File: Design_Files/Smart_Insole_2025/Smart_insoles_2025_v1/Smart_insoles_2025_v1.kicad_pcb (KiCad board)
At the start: 4 copper layers, 69.7 x 30.1 mm, 88 parts, among them IC1 USBLC6-2SC6, J1 Conn_01x20, J2 USB_C_Receptacle_USB2.0_16P, J4 S2B-PH-SM4-TB_LF__SN_, Q2 FDN306P, SW1 RESET, SW2 BOOT, SW3 SW_Nidec_CAS-120A1, U1 ME6211C33M5, U2 CD74HC4067M96, U3 LSM6DSO32TR, U5 ESP32-C3-MINI-1-N4, U7 BQ24040DSQR, U8 MCP6004-I_ST, U9 MCP6004-I_ST

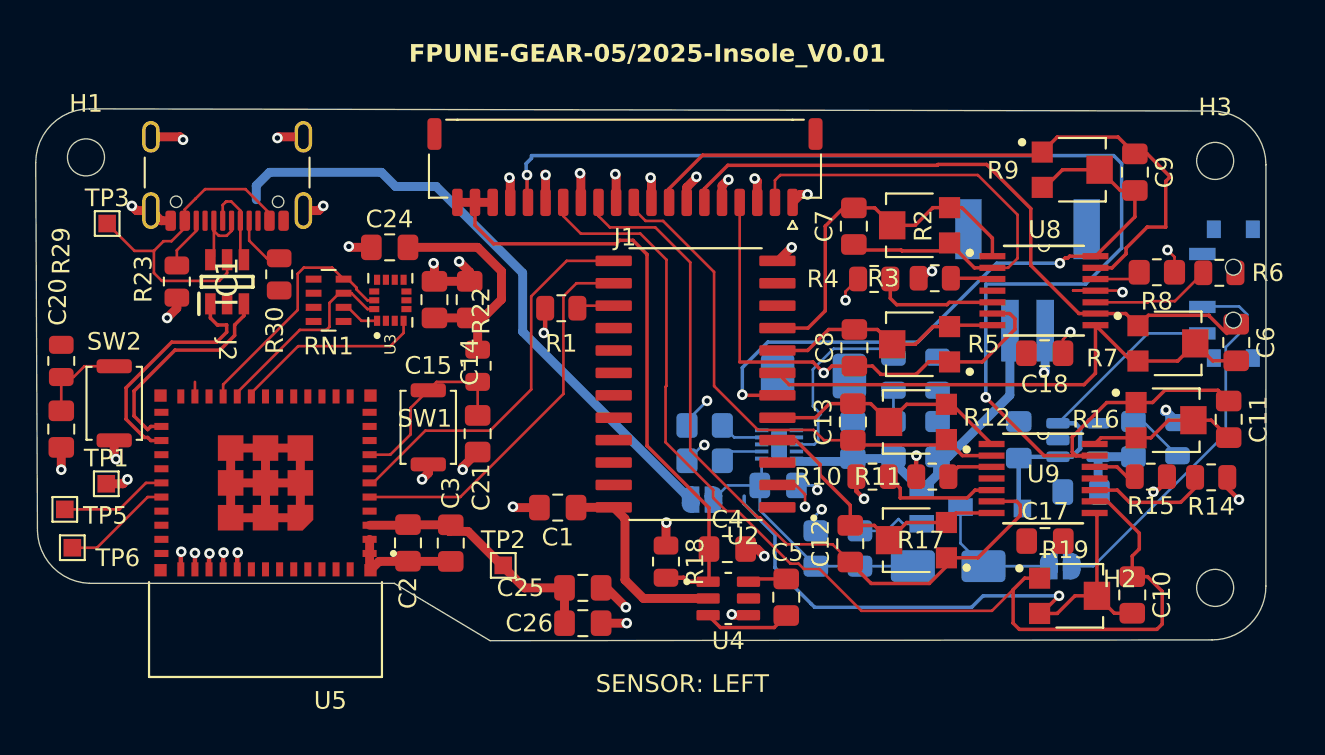
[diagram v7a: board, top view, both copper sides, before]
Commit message: PCB:Routing missing connection. Still some missing
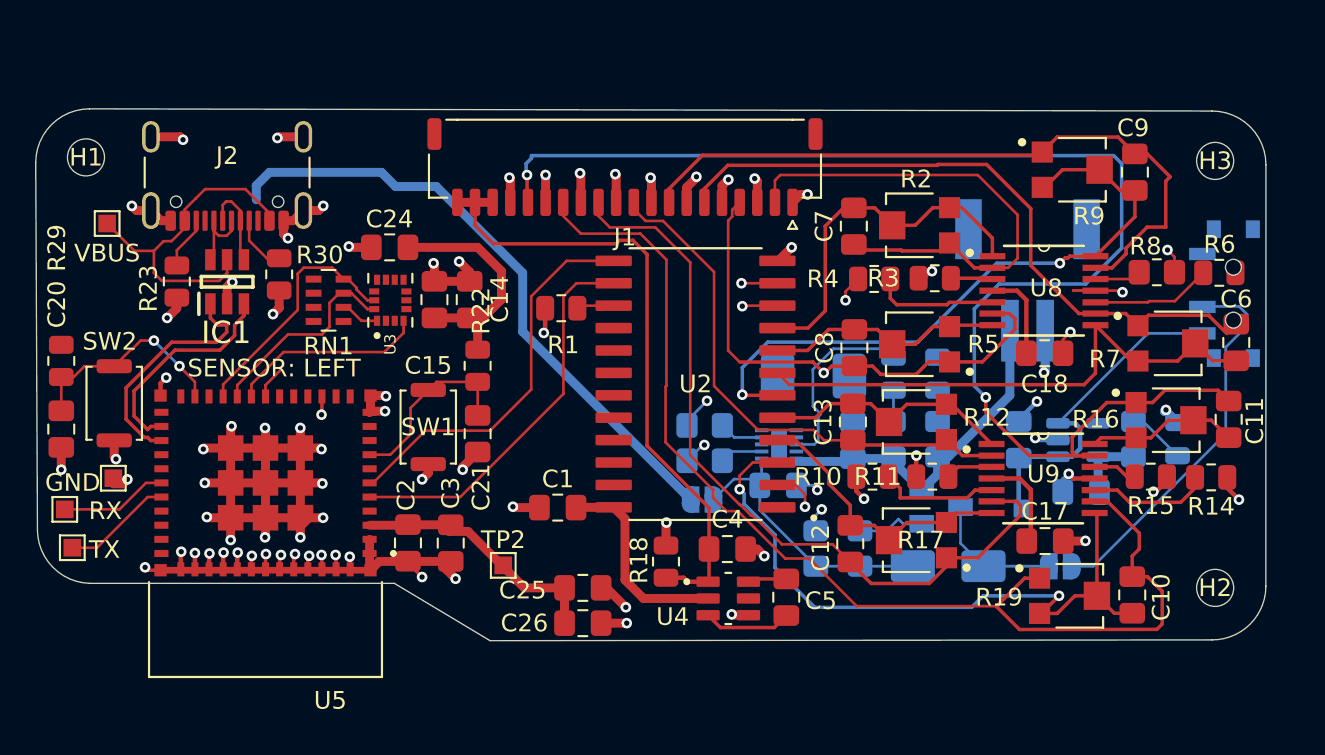
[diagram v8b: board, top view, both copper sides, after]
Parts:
- moved GND 0.51 mm to (109.2, 89.8)
- renumbered TP1 to GND, TP5 to RX, TP6 to TX, TP3 to VBUS
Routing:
- net GND: track 104.1 -> 159.3 mm, vias 50 -> 84
- net +3V3: track 45.1 -> 55.8 mm
- net Net-(U5-IO9): track 5.99 -> 12.1 mm, vias 0 -> 2
- net I6: track 34.4 -> 38.1 mm, vias 1 -> 2
- net S1: track 0.00 -> 2.04 mm, vias 0 -> 1
- net S0: track 0.00 -> 2.00 mm, vias 0 -> 1
- net SIG: track 0.00 -> 1.88 mm
- net /FSR_AnalogFE/FSR_OUT_7: track 76.2 -> 76.8 mm
- net /FSR_AnalogFE/FSR_OUT_6: track 64.6 -> 65.2 mm
- net /FSR_AnalogFE/FSR_OUT_1: track 28.3 -> 28.9 mm
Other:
- board text added: "FPUNE-GEAR Insole_V0.01 05/2025"
- board text removed: "FPUNE-GEAR-05/2025-Insole_V0.01"
